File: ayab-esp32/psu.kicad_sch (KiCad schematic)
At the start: 45 parts, among them J602 Brother_5P, J604 Brother_4R, U401 XL1509, U402 XL1509

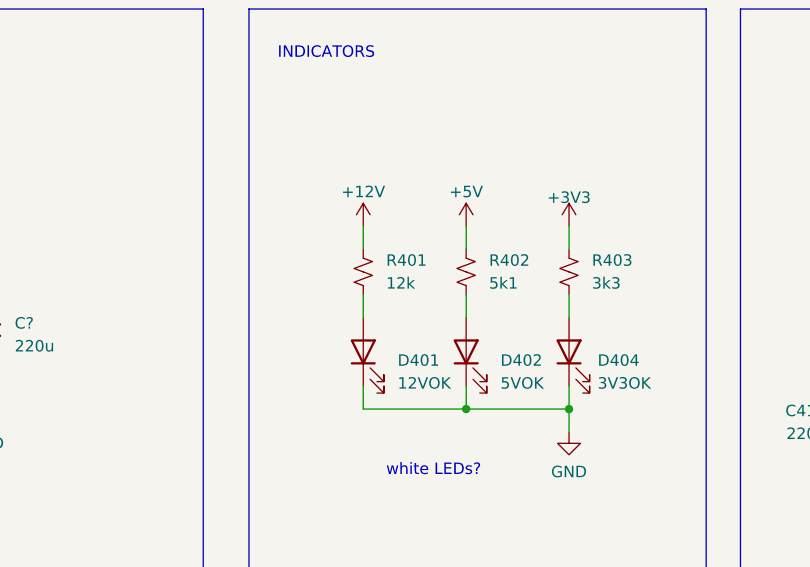
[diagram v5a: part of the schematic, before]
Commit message: Correct footprint and regenerate documentation
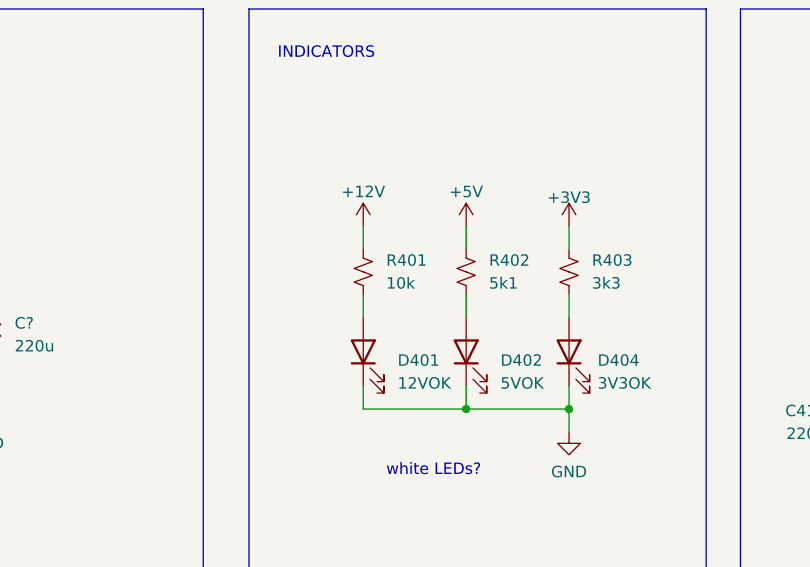
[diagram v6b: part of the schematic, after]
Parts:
- D405, D406: LCSC ID C2290 -> C22452; OEM Hubei KENTO Elec -> (none)
- R401: value 12k -> 10k; LCSC ID C22790 -> C25804; OEM PN 0603WAF1202T5E -> 0603WAF1002T5E
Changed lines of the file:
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@@
       (effects (font (size 1.27 1.27)) (justify left))
     )
-    (property "Value" "12k" (at 113.03 119.38 0)
+    (property "Value" "10k" (at 113.03 119.38 0)
       (effects (font (size 1.27 1.27)) (justify left))
     )
@@
       (effects (font (size 1.27 1.27)) hide)
     )
-    (property "LCSC ID" "C22790" (at 110.49 118.11 0)
-      (effects (font (size 1.27 1.27)) hide)
-    )
-    (property "OEM PN" "0603WAF1202T5E" (at 110.49 118.11 0)
+    (property "LCSC ID" "C25804" (at 110.49 118.11 0)
+      (effects (font (size 1.27 1.27)) hide)
+    )
+    (property "OEM PN" "0603WAF1002T5E" (at 110.49 118.11 0)
       (effects (font (size 1.27 1.27)) hide)
     )
@@
       (effects (font (size 1.27 1.27)) hide)
     )
-    (property "LCSC ID" "C2290" (at 214.63 134.62 0)
+    (property "LCSC ID" "C22452" (at 214.63 134.62 0)
       (effects (font (size 1.27 1.27)) hide)
     )
@@
       (effects (font (size 1.27 1.27)) hide)
     )
-    (property "OEM" "Hubei KENTO Elec" (at 214.63 134.62 0)
+    (property "OEM" "" (at 214.63 134.62 0)
       (effects (font (size 1.27 1.27)) hide)
     )
@@
       (effects (font (size 1.27 1.27)) hide)
     )
-    (property "LCSC ID" "C2290" (at 214.63 60.96 0)
+    (property "LCSC ID" "C22452" (at 214.63 60.96 0)
       (effects (font (size 1.27 1.27)) hide)
     )
@@
       (effects (font (size 1.27 1.27)) hide)
     )
-    (property "OEM" "Hubei KENTO Elec" (at 214.63 60.96 0)
-      (effects (font (size 1.27 1.27)) hide)
-    )
+    (property "OEM" "" (at 214.63 60.96 0)
+      (effects (font (size 1.27 1.27)) hide)
+    )

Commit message: add mouser parts list
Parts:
- C415, C420, C421, C? (x2): Mouser PN (none) -> 661-EMZR250ARA221MF8
- C416, C417, C? (x11): Mouser PN (none) -> 963-TMK212BBJ106KG-T
- C418, C419: Mouser PN (none) -> 80-C0603C332K2RACTU
- D401, D402, D404: Mouser PN (none) -> 696-SML-LXT0805IW
- D405, D406: Mouser PN (none) -> 750-SS54B-HF
- J?: Mouser PN (none) -> 806-KLDXSMT20202BT
- L401, L402: Mouser PN (none) -> 580-49470SC
- R401: Mouser PN (none) -> 791-RMC16K103FTP
- R402: Mouser PN (none) -> 603-AC0603FR-135K1L
- R403, R406: Mouser PN (none) -> 603-RC0603FR-073K3P
- R404, R405: Mouser PN (none) -> 71-CRCW06031K24FKEAC
- R406: Mouser PN (none) -> 71-CRCW06030000Z0EC
- R407: Mouser PN (none) -> 279-CRG0603F1K8

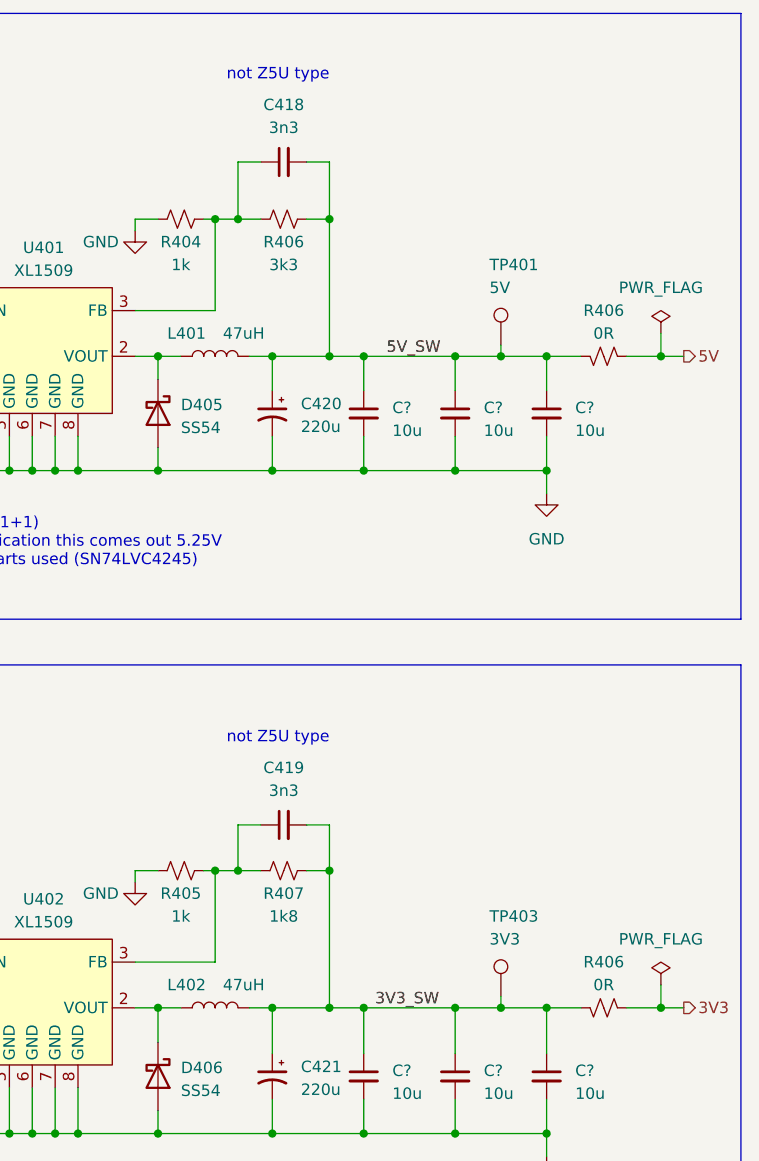
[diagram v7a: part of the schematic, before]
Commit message: address bringup issues
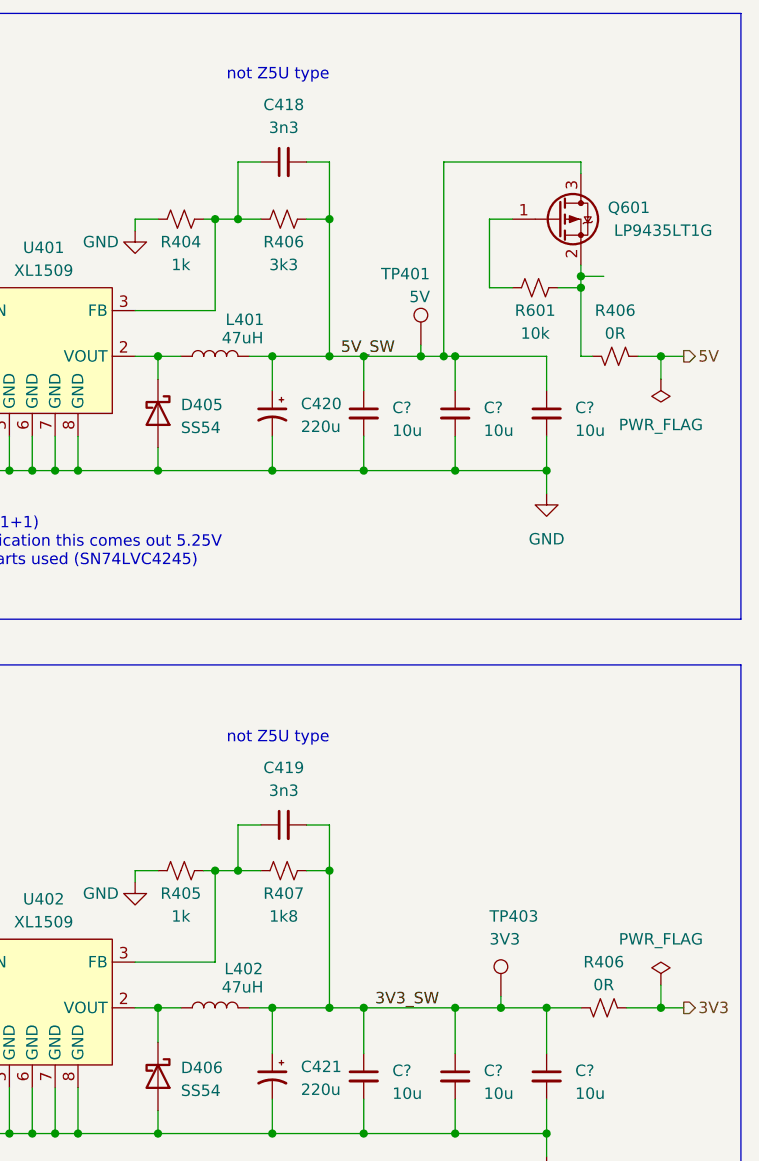
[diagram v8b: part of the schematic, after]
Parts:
- added Q601: LP9435LT1G, Package_TO_SOT_SMD:SOT-23, symbol ayab-lib:AO3401A
- added R601: 10k, Resistor_SMD:R_0603_1608Metric, symbol ayab-lib:R_Small_US
- R406: footprint Resistor_SMD:R_0603_1608Metric -> Resistor_SMD:R_0805_2012Metric; LCSC ID C21189 -> C17477
- U401, U402: LCSC ID C61063 -> C74192
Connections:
- net 5V_SW: now also Q601.3 (D); no longer R406.1
- new net: Q601.2 (S), R406.1, R601.2
- new net: Q601.1 (G), R601.1
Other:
- moved on the sheet: R406, TP401
